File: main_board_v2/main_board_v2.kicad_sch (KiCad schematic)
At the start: 1 part

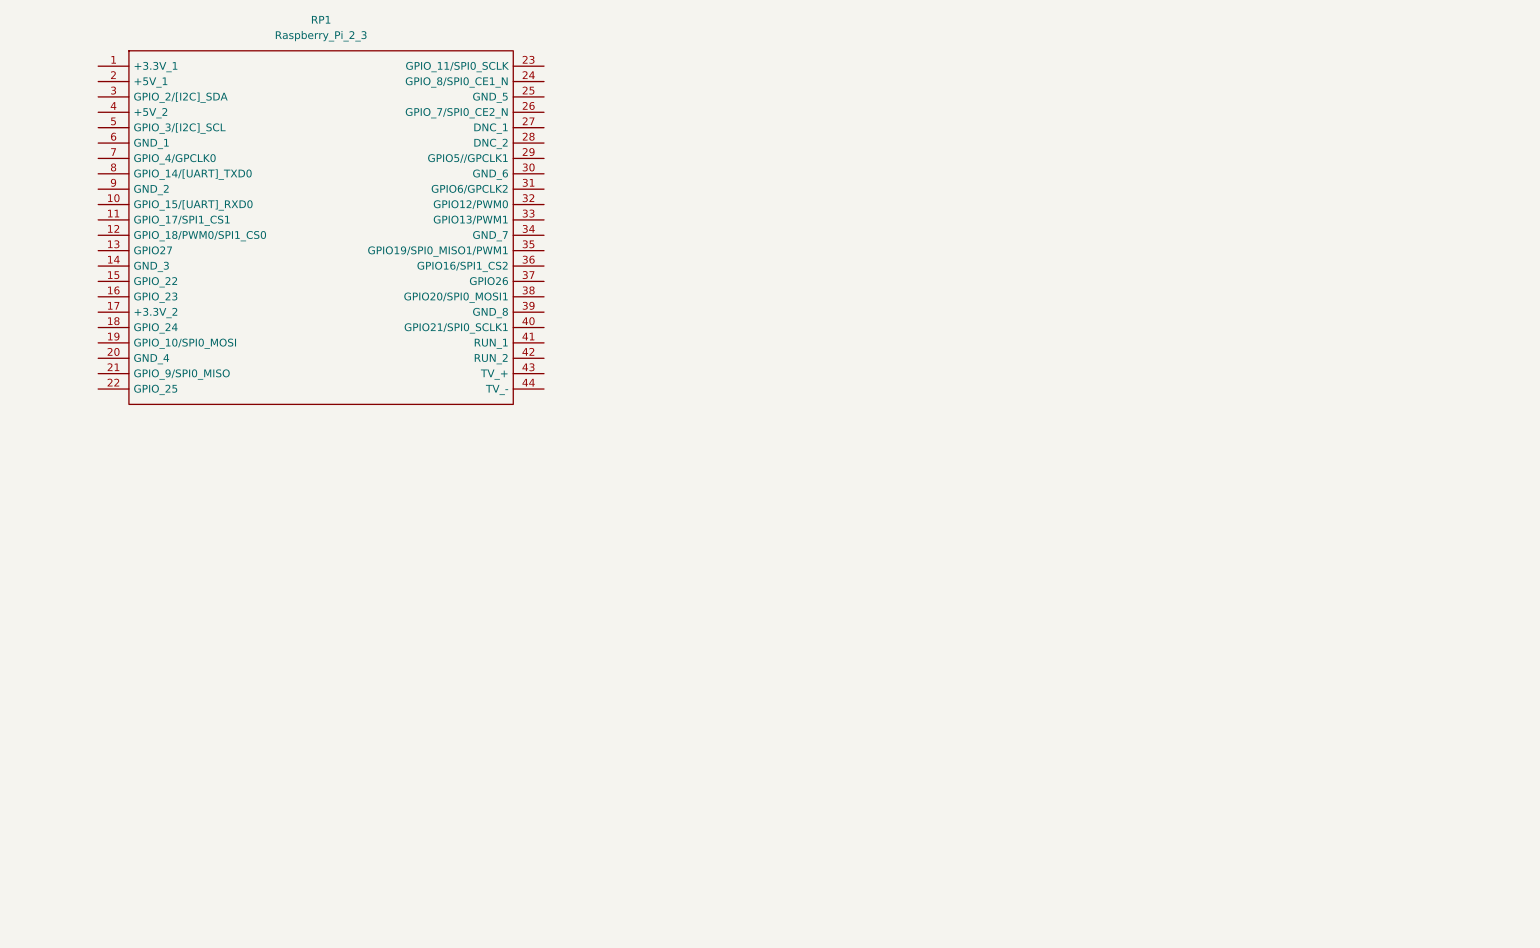
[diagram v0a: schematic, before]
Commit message: Added traco and tdk regulators, and IMU and more
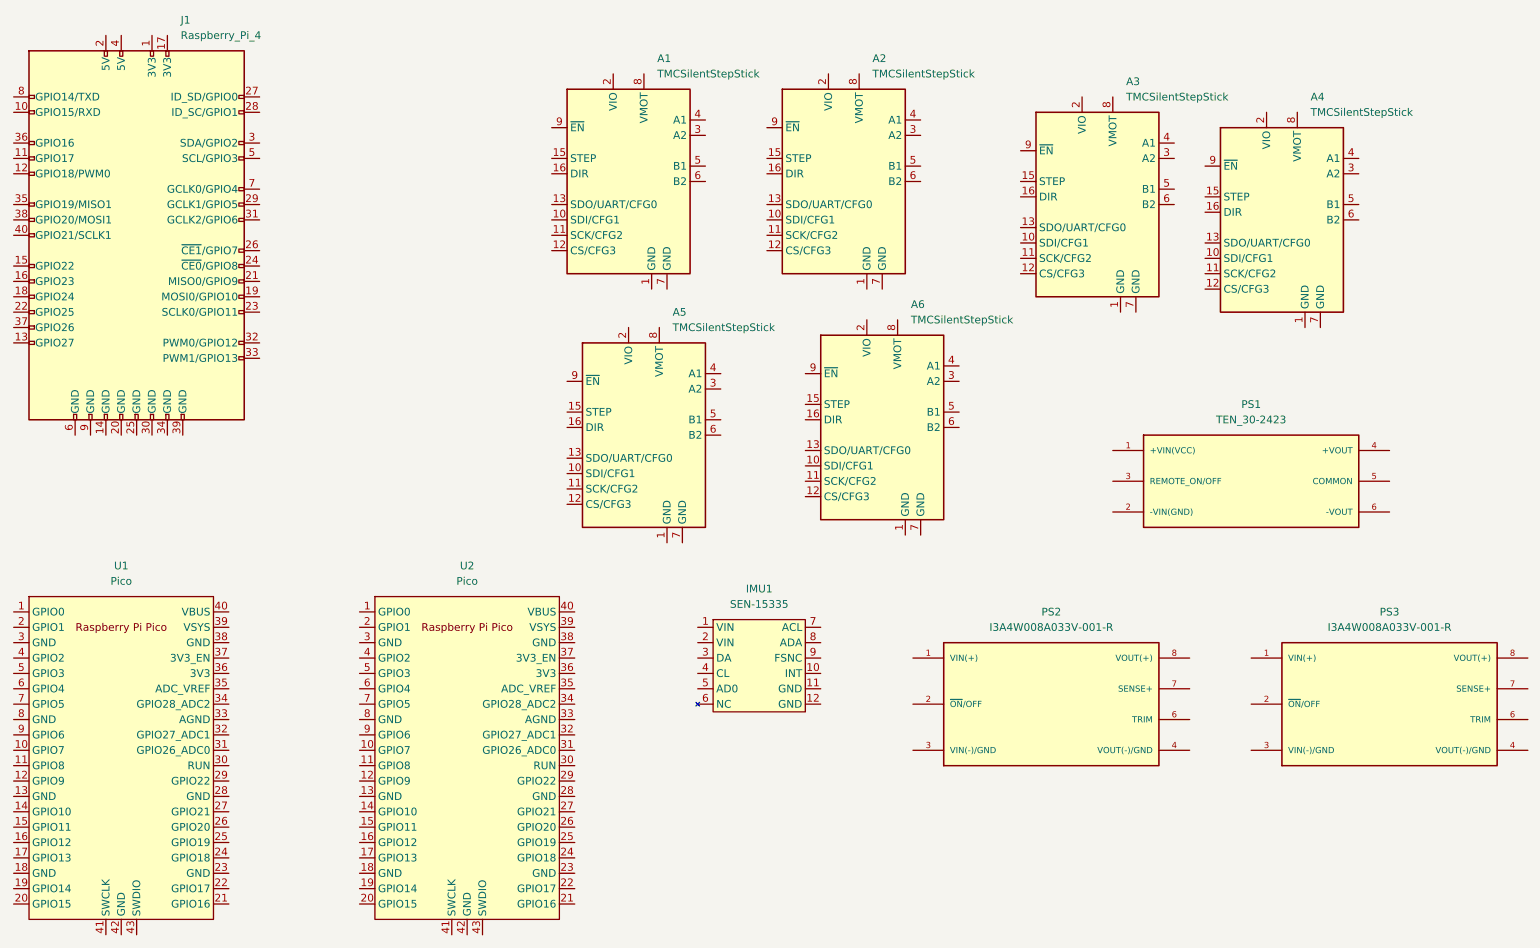
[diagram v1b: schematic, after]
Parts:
- removed RP1: Raspberry_Pi_2_3, RASPBERRYPI, symbol Raspberry_Pi_2_or_3:Raspberry_Pi_2_3
- added A1, A2, A3, A4, A5, A6: TMCSilentStepStick, Ensmasteel_librairy:TMCStick, symbol ENSMASTEEL_librairy:TMCSilentStepStick
- added IMU1: SEN-15335, Ensmasteel_librairy:SEN-15335, symbol ENSMASTEEL_librairy:SEN-15335
- added J1: Raspberry_Pi_4, Ensmasteel_librairy:Raspberry_Pi_4, symbol ENSMASTEEL_librairy:Raspberry_Pi_4
- added PS1: TEN_30-2423, Ensmasteel_librairy:CONV_TEN_30-2423, symbol ENSMASTEEL_librairy:TEN_30-2423
- added PS2, PS3: I3A4W008A033V-001-R, Ensmasteel_librairy:CONV_I3A4W008A033V-001-R, symbol ENSMASTEEL_librairy:I3A4W008A033V-001-R
- added U1, U2: Pico, Ensmasteel_librairy:RPi_Pico_SMD_TH, symbol ENSMASTEEL_librairy:Pico

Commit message: Work, lots of
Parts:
- removed A5, A6: TMCSilentStepStick, Ensmasteel_librairy:TMCStick, symbol ENSMASTEEL_librairy:TMCSilentStepStick
- added BAU1: XT60-F, Connector_AMASS:AMASS_XT60-F_1x02_P7.20mm_Vertical, symbol Connector:Conn_01x02_Pin
- added Battery1: XT60-M, Connector_AMASS:AMASS_XT60-M_1x02_P7.20mm_Vertical, symbol Connector:Conn_01x02_Pin
- added C1, C10, C11, C12, C3, C4, C5, C6, C7, C8, C9: 100uF, Capacitor_THT:C_Radial_D6.3mm_H11.0mm_P2.50mm, symbol Device:C_Polarized
- added C13, C14, C2: 1uF, Capacitor_SMD:C_0201_0603Metric, symbol Device:C
- added ERR1, ERR2, ERR3, TiretteOK1: LED, LED_SMD:LED_0805_2012Metric, symbol Device:LED
- added F1: Fuse, Fuse:Fuseholder_Blade_ATO_Littelfuse_Pudenz_2_Pin, symbol Device:Fuse
- added JP1, JP2, JP3: SolderJumper_2_Open, Jumper:SolderJumper-2_P1.3mm_Open_RoundedPad1.0x1.5mm, symbol Jumper:SolderJumper_2_Open
- added LEDStrip1, PICO1_UART1, PICO1_swd1, PICO2_I2C1, PICO2_swd1, RPI_PWMs1, RPI_serial1: JST PH 3, Connector_JST:JST_PH_B3B-PH-K_1x03_P2.00mm_Vertical, symbol Connector:Conn_01x03_Pin
- added R1, R2, R3, R4: 100R, Resistor_SMD:R_0201_0603Metric, symbol Device:R
- added R3 (x2): R_Trim, Potentiometer_THT:Potentiometer_Bourns_3296X_Horizontal, symbol Device:R_Trim
- added R5: 1k, Resistor_THT:R_Axial_DIN0207_L6.3mm_D2.5mm_P10.16mm_Horizontal, symbol Device:R
- added RPI_SPI1, Stepper1, Stepper2, Stepper3, Stepper4, Tirette1: jst PH 01x4, Connector_JST:JST_PH_B4B-PH-K_1x04_P2.00mm_Vertical, symbol Connector:Conn_01x04_Pin
- added Servo1, Servo10, Servo11, Servo12, Servo2, Servo3, Servo4, Servo5, Servo6, Servo7, Servo8, Servo9: 1x3_PinHeader, Connector_PinHeader_2.54mm:PinHeader_1x03_P2.54mm_Vertical, symbol Connector:Conn_01x03_Pin
- added U1: 4N25, OptoDevice:Luna_NSL-32, symbol Isolator:4N25
- PS3: renamed from PS1; value TEN_30-2423 -> TEN_50-2423
- renumbered PS2 to PS1, PS3 to PS2, U1 to U2, U2 to U3
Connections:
- net GND: now reaches A2.1 (GND)
- net GND: now also A1.1 (GND), A1.7 (GND), A2.7 (GND), A3.1 (GND), A3.7 (GND), A4.1 (GND), A4.7 (GND), IMU1.11 (GND), IMU1.12 (GND), J1.14 (GND), J1.20 (GND), J1.25 (GND), J1.30 (GND), J1.34 (GND), J1.39 (GND), J1.6 (GND), J1.9 (GND), PS1.2 (~{ON}/OFF), PS1.3 (VIN(-)/GND), PS1.4 (VOUT(-)/GND), PS2.2 (~{ON}/OFF), PS2.3 (VIN(-)/GND), PS2.4 (VOUT(-)/GND), PS3.2 (-VIN(GND)), PS3.6 (-VOUT), U2.13 (GND), U2.18 (GND), U2.23 (GND), U2.28 (GND), U2.3 (GND), U2.38 (GND), U2.42 (GND), U2.8 (GND), U3.13 (GND), U3.18 (GND), U3.23 (GND), U3.28 (GND), U3.3 (GND), U3.38 (GND), U3.42 (GND), U3.8 (GND), Battery1.1 (Pin_1), C1.2, C10.2, C11.2, C12.2, C13.2, C14.2, C2.1, C3.2, C4.2, C5.2, C6.2, C7.2, C8.2, C9.2, LEDStrip1.3 (Pin_3), PICO1_UART1.3 (Pin_3), PICO1_swd1.2 (Pin_2), PICO2_I2C1.1 (Pin_1), PICO2_swd1.2 (Pin_2), R1.1, R2.1, R3.1, R3.2, R3.2, R4.1, R5.2, RPI_PWMs1.1 (Pin_1), RPI_SPI1.1 (Pin_1), RPI_serial1.3 (Pin_3), Servo1.1 (Pin_1), Servo10.1 (Pin_1), Servo11.1 (Pin_1), Servo12.1 (Pin_1), Servo2.1 (Pin_1), Servo3.1 (Pin_1), Servo4.1 (Pin_1), Servo5.1 (Pin_1), Servo6.1 (Pin_1), Servo7.1 (Pin_1), Servo8.1 (Pin_1), Servo9.1 (Pin_1), Tirette1.1 (Pin_1), U1.2
- net CFG1: now reaches A2.10 (SDI/CFG1)
- net CFG1: now also A1.10 (SDI/CFG1), A3.10 (SDI/CFG1), A4.10 (SDI/CFG1), JP2.1 (A)
- net CFG2: now reaches A2.11 (SCK/CFG2)
- net CFG2: now also A1.11 (SCK/CFG2), A3.11 (SCK/CFG2), A4.11 (SCK/CFG2), JP1.1 (A)
- net CFG3: now reaches A2.12 (CS/CFG3)
- net CFG3: now also A1.12 (CS/CFG3), A3.12 (CS/CFG3), A4.12 (CS/CFG3), U2.9 (GPIO6)
- net CFG0: now reaches A2.13 (SDO/UART/CFG0)
- net CFG0: now also A1.13 (SDO/UART/CFG0), A3.13 (SDO/UART/CFG0), A4.13 (SDO/UART/CFG0), JP3.1 (A)
- net STEP3: now reaches A2.15 (STEP)
- net STEP3: now also U2.15 (GPIO11)
- net DIR3: now reaches A2.16 (DIR)
- net DIR3: now also U2.16 (GPIO12)
- net VIO_stepper_drivers: now reaches A2.2 (VIO)
- net VIO_stepper_drivers: now also A1.2 (VIO), A3.2 (VIO), A4.2 (VIO)
- net at A2.3 (A2): now also Stepper2.2 (Pin_2)
- net at A2.4 (A1): now also Stepper2.1 (Pin_1)
- net at A2.5 (B1): now also Stepper2.3 (Pin_3)
- net at A2.6 (B2): now also Stepper2.4 (Pin_4)
- net FusedProtectedVbatt: now reaches A2.8 (VMOT)
- net FusedProtectedVbatt: now also A1.8 (VMOT), A3.8 (VMOT), A4.8 (VMOT), C10.1, C11.1, C12.1, C9.1, F1.2
- net EN: now reaches A2.9 (~{EN})
- net EN: now also A1.9 (~{EN}), A3.9 (~{EN}), A4.9 (~{EN}), U2.4 (GPIO2)
- net RPI_pico2_TX0: now reaches U3.1 (GPIO0)
- net servo3: now reaches U3.10 (GPIO7)
- net servo3: now also Servo8.3 (Pin_3)
- net servo4: now reaches U3.11 (GPIO8)
- net servo4: now also Servo3.3 (Pin_3)
- net servo5: now reaches U3.12 (GPIO9)
- net servo5: now also Servo9.3 (Pin_3)
- net servo6: now reaches U3.14 (GPIO10)
- net servo6: now also Servo4.3 (Pin_3)
- net servo7: now reaches U3.15 (GPIO11)
- net servo7: now also Servo10.3 (Pin_3)
- net servo8: now reaches U3.16 (GPIO12)
- net servo8: now also Servo5.3 (Pin_3)
- net servo9: now reaches U3.17 (GPIO13)
- net servo9: now also Servo11.3 (Pin_3)
- net servo10: now reaches U3.19 (GPIO14)
- net servo10: now also Servo6.3 (Pin_3)
- net RPI_pico2_RX0: now reaches U3.2 (GPIO1)
- net servo11: now reaches U3.20 (GPIO15)
- net servo11: now also Servo12.3 (Pin_3)
- net ISC1_SDA: now reaches U3.31 (GPIO26_ADC0)
- net ISC1_SDA: now also PICO2_I2C1.3 (Pin_3)
- net ISC1_SCL: now reaches U3.32 (GPIO27_ADC1)
- net ISC1_SCL: now also PICO2_I2C1.2 (Pin_2)
- net servo0: now reaches U3.4 (GPIO2)
- net servo0: now also Servo1.3 (Pin_3)
- net +5V: now reaches U3.40 (VBUS)
- net +5V: now also J1.2 (5V), J1.4 (5V), PS3.4 (+VOUT), U2.40 (VBUS), C1.1, C13.1, C14.1, C2.2, C6.1
- net at U3.41 (SWCLK): now also PICO2_swd1.1 (Pin_1)
- net at U3.43 (SWDIO): now also PICO2_swd1.3 (Pin_3)
- net servo1: now reaches U3.5 (GPIO3)
- net servo1: now also Servo7.3 (Pin_3)
- net RPI_RX4: now reaches U3.6 (GPIO4)
- net RPI_RX4: now also J1.21 (MISO0/GPIO9)
- net RPI_TX4: now reaches U3.7 (GPIO5)
- net RPI_TX4: now also J1.24 (~{CE0}/GPIO8)
- net servo2: now reaches U3.9 (GPIO6)
- net servo2: now also Servo2.3 (Pin_3)
- net +BATT: now reaches PS3.1 (+VIN(VCC))
- net +BATT: now also BAU1.2 (Pin_2), Battery1.2 (Pin_2), C5.1, Tirette1.4 (Pin_4)
- net STEP4: now reaches A3.15 (STEP)
- net STEP4: now also U2.17 (GPIO13)
- net DIR4: now reaches A3.16 (DIR)
- net DIR4: now also U2.19 (GPIO14)
- net at A3.3 (A2): now also Stepper3.2 (Pin_2)
- net at A3.4 (A1): now also Stepper3.1 (Pin_1)
- net at A3.5 (B1): now also Stepper3.3 (Pin_3)
- net at A3.6 (B2): now also Stepper3.4 (Pin_4)
- net RPI_pico1_TX0: now reaches U2.1 (GPIO0)
- net RPI_pico1_TX0: now also PICO1_UART1.2 (Pin_2)
- net STEP1: now reaches U2.10 (GPIO7)
- net STEP1: now also A1.15 (STEP)
- net DIR1: now reaches U2.11 (GPIO8)
- net DIR1: now also A1.16 (DIR)
- net STEP2: now reaches U2.12 (GPIO9)
- net STEP2: now also A4.15 (STEP)
- net DIR2: now reaches U2.14 (GPIO10)
- net DIR2: now also A4.16 (DIR)
- net RPI_pico1_RX0: now reaches U2.2 (GPIO1)
- net RPI_pico1_RX0: now also PICO1_UART1.1 (Pin_1)
- net at U2.25 (GPIO19): now also JP3.2 (B)
- net at U2.26 (GPIO20): now also JP2.2 (B)
- net at U2.27 (GPIO21): now also JP1.2 (B)
- net at U2.41 (SWCLK): now also PICO1_swd1.1 (Pin_1)
- net at U2.43 (SWDIO): now also PICO1_swd1.3 (Pin_3)
- net RPI_RX3: now reaches U2.6 (GPIO4)
- net RPI_RX3: now also J1.29 (GCLK1/GPIO5)
- net RPI_TX3: now reaches U2.7 (GPIO5)
- net RPI_TX3: now also J1.7 (GCLK0/GPIO4)
- net at A4.3 (A2): now also Stepper4.2 (Pin_2)
- net at A4.4 (A1): now also Stepper4.1 (Pin_1)
- net at A4.5 (B1): now also Stepper4.3 (Pin_3)
- net at A4.6 (B2): now also Stepper4.4 (Pin_4)
- net ProtectedVbatt: now reaches PS2.1 (VIN(+))
- net ProtectedVbatt: now also PS1.1 (VIN(+)), BAU1.1 (Pin_1), C3.1, C4.1, F1.1
- net at PS2.6 (TRIM): now also R3.1
- net +5VP: now reaches PS2.7 (SENSE+)
- net +5VP: now also PS2.8 (VOUT(+)), C8.1, LEDStrip1.1 (Pin_1), Servo1.2 (Pin_2), Servo2.2 (Pin_2), Servo3.2 (Pin_2), Servo7.2 (Pin_2), Servo8.2 (Pin_2), Servo9.2 (Pin_2)
- net +3.3V: now reaches IMU1.1 (VIN)
- net +3.3V: now also IMU1.2 (VIN), J1.1 (3V3), J1.17 (3V3), U1.5
- net PI_SDA: now reaches IMU1.3 (DA)
- net PI_SDA: now also J1.3 (SDA/GPIO2)
- net PI_SCL: now reaches IMU1.4 (CL)
- net PI_SCL: now also J1.5 (SCL/GPIO3)
- net at A1.3 (A2): now also Stepper1.2 (Pin_2)
- net at A1.4 (A1): now also Stepper1.1 (Pin_1)
- net at A1.5 (B1): now also Stepper1.3 (Pin_3)
- net at A1.6 (B2): now also Stepper1.4 (Pin_4)
- net at PS1.6 (TRIM): now also R3.1
- net +7.5V: now reaches PS1.7 (SENSE+)
- net +7.5V: now also PS1.8 (VOUT(+)), C7.1, Servo10.2 (Pin_2), Servo11.2 (Pin_2), Servo12.2 (Pin_2), Servo4.2 (Pin_2), Servo5.2 (Pin_2), Servo6.2 (Pin_2)
- net at J1.10 (GPIO15/RXD): now also RPI_serial1.2 (Pin_2)
- net TIRETTE_input: now reaches J1.15 (GPIO22)
- net TIRETTE_input: now also R5.1, U1.4
- net at J1.16 (GPIO23): now also TiretteOK1.2 (A)
- net at J1.18 (GPIO24): now also ERR1.2 (A)
- net at J1.22 (GPIO25): now also ERR2.2 (A)
- net at J1.32 (PWM0/GPIO12): now also RPI_PWMs1.3 (Pin_3)
- net at J1.33 (PWM1/GPIO13): now also RPI_PWMs1.2 (Pin_2)
- net at J1.35 (GPIO19/MISO1): now also RPI_SPI1.4 (Pin_4)
- net LED_strip: now reaches J1.36 (GPIO16)
- net LED_strip: now also LEDStrip1.2 (Pin_2)
- net at J1.37 (GPIO26): now also ERR3.2 (A)
- net at J1.38 (GPIO20/MOSI1): now also RPI_SPI1.3 (Pin_3)
- net at J1.40 (GPIO21/SCLK1): now also RPI_SPI1.2 (Pin_2)
- net at J1.8 (GPIO14/TXD): now also RPI_serial1.1 (Pin_1)
- new net: R1.2, TiretteOK1.1 (K)
- new net: ERR2.1 (K), R3.2
- new net: Tirette1.3 (Pin_3), U1.1
- new net: ERR3.1 (K), R4.2
- new net: ERR1.1 (K), R2.2
- no-connect marks 0 -> 2
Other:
- note added: "5V servos"
- note added: "7.4V servos"
- note added: "https://micro.ros.org/docs/tutorials/core/first_application_rtos/freertos/"
- moved on the sheet: A1, IMU1, J1, PS1, PS2, PS3, U2, U3
